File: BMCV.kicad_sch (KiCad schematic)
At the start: 32 parts, among them J13 DebugPins, J14 USB_C_Receptacle_USB2.0_14P, J15 Conn_01x02, SW14 Reset, SW15 Boot, U32 TXS0108EPW, U36 STM32G474CETx, U37 MB85RS64PNF-G-JNERE1, Y1 38.4MHz 10pF

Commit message: update
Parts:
- removed J15: Conn_01x02, TestPoint:TestPoint_2Pads_Pitch2.54mm_Drill0.8mm, symbol PCM_4ms_Connector:Conn_01x02
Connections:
- net PB7 is gone; now on net LEVEL_SHIFTER_EN: U36.44 (PB7)
- net +3.3V: no longer R162.2
- net GND: now also R162.1
- net LEVEL_SHIFTER_EN: now reaches U32.10 (OE)
- net LEVEL_SHIFTER_EN: now also R162.2; no longer R162.1
- net PB6 renamed PWR_ANALOG_EN
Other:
- moved on the sheet: R162

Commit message: first ordered verrsion
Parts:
- added R4: 1k5, Resistor_SMD:R_0603_1608Metric, symbol Device:R_Small
- C1, C2: LCSC Part # C32949 -> C161520
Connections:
- net +3.3VA: now also U36.20 (VREF+)
- net GND: now also VR1.E1 (E_(-))
- net at VR1.B1 (B_(+)): now also R4.2
- net PWR_ANALOG_EN renamed SLIDER_LED
- net SLIDER_LED: now also R4.1
- no-connect marks 6 -> 3
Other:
- note added: "NRST/PG10 has internal pull-up"

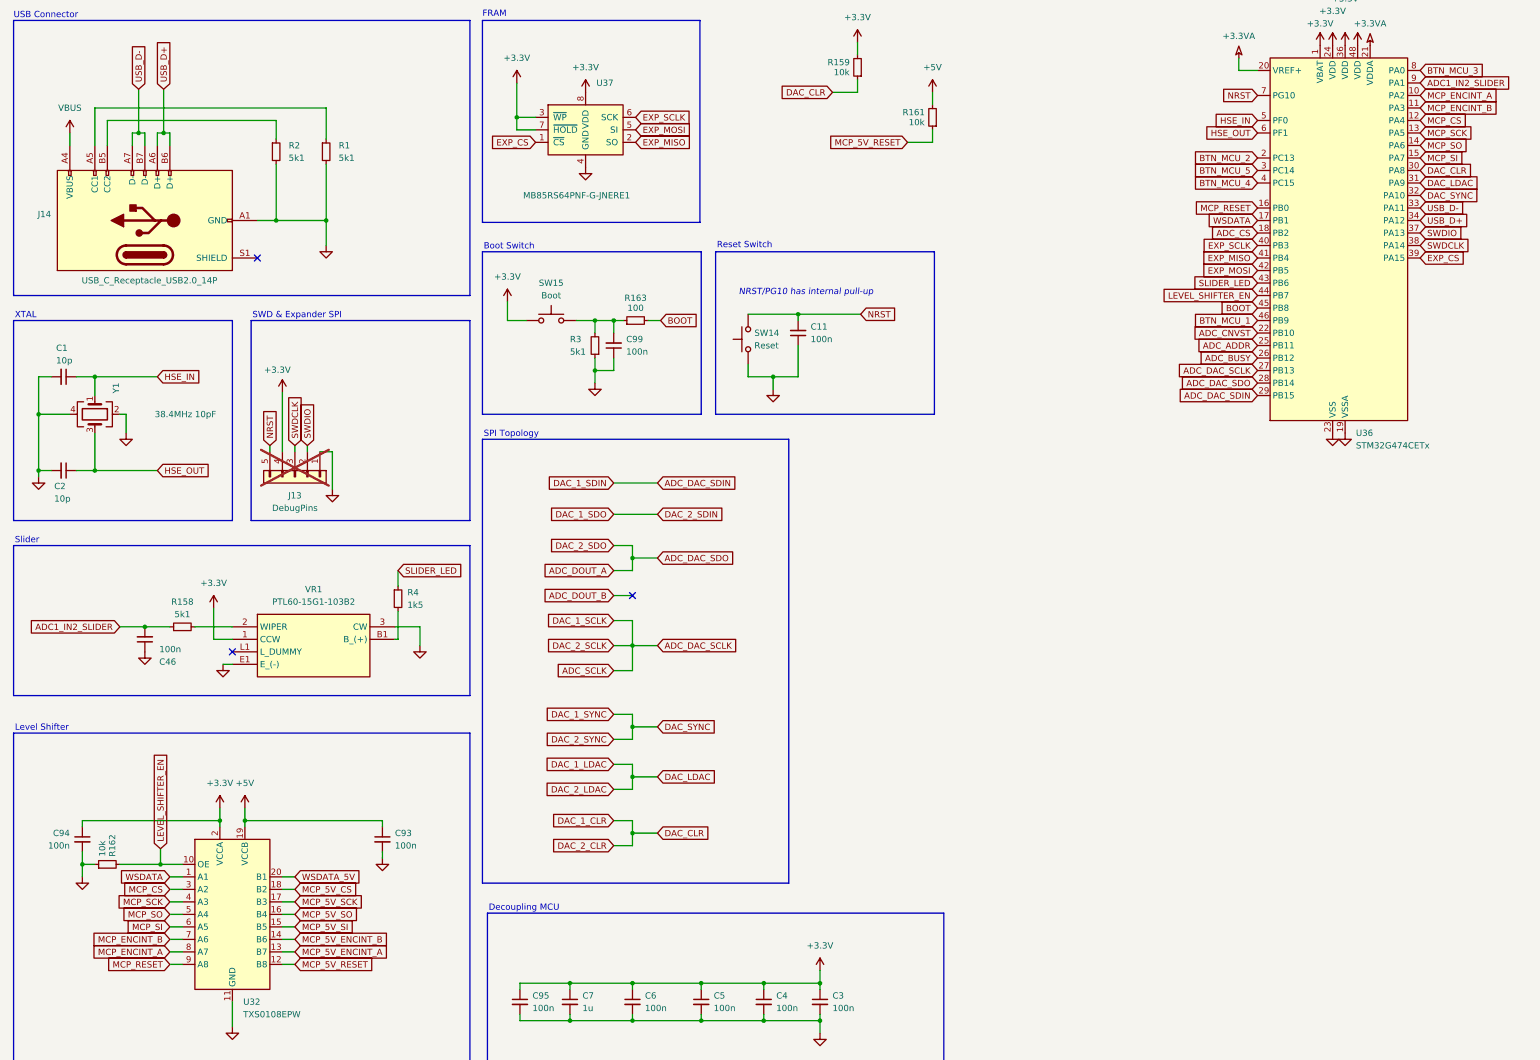
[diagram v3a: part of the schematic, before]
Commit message: add test firwmware
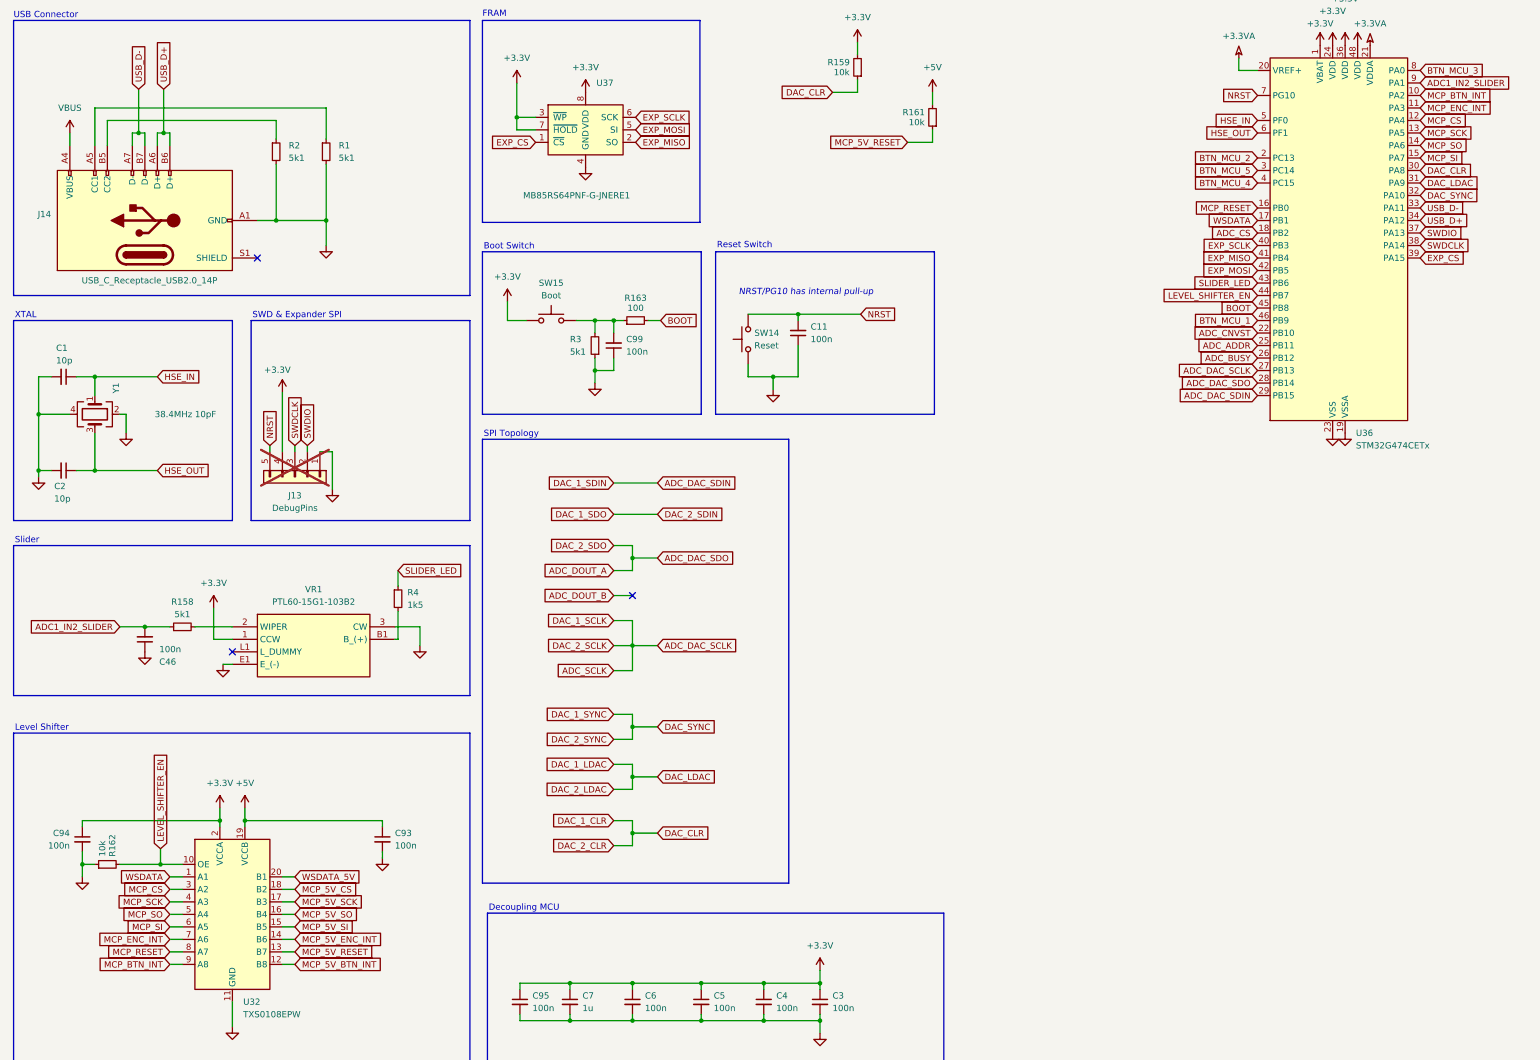
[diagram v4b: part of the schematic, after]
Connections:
- net MCP_5V_ENCINT_A is gone; now on net MCP_5V_RESET: U32.13 (B7)
- net MCP_5V_RESET: no longer U32.12 (B8)
- net MCP_RESET: now also U32.8 (A7); no longer U32.9 (A8)
- net MCP_5V_ENCINT_B renamed MCP_5V_ENC_INT
- net MCP_ENCINT_A renamed MCP_BTN_INT
- net MCP_BTN_INT: now also U32.9 (A8); no longer U32.8 (A7)
- net MCP_ENCINT_B renamed MCP_ENC_INT
- new net MCP_5V_BTN_INT: U32.12 (B8)

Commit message: pcb changes
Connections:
- no-connect marks 3 -> 4
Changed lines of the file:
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@@
 	)
 	(junction
-		(at 140.97 175.26)
-		(diameter 0)
-		(color 0 0 0 0)
-	)
-	(junction
 		(at 29.21 237.49)
 		(diameter 0)
@@
 	)
 	(no_connect
+		(at 140.97 172.72)
+	)
+	(no_connect
 		(at 64.77 114.3)
 	)
@@
 	(wire
 		(pts
-			(xy 140.97 177.8) (xy 137.16 177.8)
+			(xy 137.16 177.8) (xy 146.05 177.8)
 		)
 		(stroke
@@
 	(wire
 		(pts
-			(xy 140.97 172.72) (xy 140.97 175.26)
-		)
-		(stroke
-			(width 0)
-			(type default)
-		)
-	)
-	(wire
-		(pts
 			(xy 118.11 269.24) (xy 128.27 269.24)
 		)
@@
 	(wire
 		(pts
-			(xy 140.97 175.26) (xy 146.05 175.26)
-		)
-		(stroke
-			(width 0)
-			(type default)
-		)
-	)
-	(wire
-		(pts
 			(xy 20.32 157.48) (xy 20.32 146.05)
 		)
@@
 	(wire
 		(pts
-			(xy 140.97 175.26) (xy 140.97 177.8)
-		)
-		(stroke
-			(width 0)
-			(type default)
-		)
-	)
-	(wire
-		(pts
 			(xy 69.85 257.81) (xy 72.39 257.81)
 		)
@@
 	(global_label "ADC_DAC_SDO"
 		(shape input)
-		(at 146.05 175.26 0)
+		(at 146.05 177.8 0)
 		(fields_autoplaced yes)
 		(effects
@@
 		)
 		(property "Intersheetrefs" "${INTERSHEET_REFS}"
-			(at 162.0376 175.26 0)
+			(at 162.0376 177.8 0)
 			(effects
 				(font

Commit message: pcb
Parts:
- added C112: 100n, Capacitor_SMD:C_0402_1005Metric, symbol Device:C_Small
- added U42: 74AHCT1G125, Package_TO_SOT_SMD:SOT-353_SC-70-5, symbol 74xGxx:74AHCT1G125
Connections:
- net +5V: now also C112.1, U42.5 (VCC)
- net GND: now also C112.2, U42.1, U42.3 (GND)
- net WSDATA: now also U42.2; no longer U32.1 (A1)
- net WSDATA_5V: now also U42.4; no longer U32.20 (B1)
- no-connect marks 4 -> 6

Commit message: pcb update
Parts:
- removed R159: 10k, Resistor_SMD:R_0402_1005Metric, symbol Device:R_Small
- added R164: 100, Resistor_SMD:R_0402_1005Metric, symbol Device:R_Small
- added R41: 5k1, Resistor_SMD:R_0402_1005Metric, symbol Device:R_Small
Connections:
- net DAC_1_LDAC is gone; now on net DAC_1_SYNC: U36.31 (PA9)
- net +3.3V: now also SW14.1
- net DAC_1_SYNC: no longer U36.32 (PA10)
- net GND: now also R41.1; no longer SW14.1
- net NRST: no longer C11.2, SW14.2
- net DAC_1_CLR renamed BTN_MENU_2
- net BTN_MENU_2: now also R164.2
- new net: C11.2, R164.1, R41.2, SW14.2
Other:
- moved on the sheet: C11, R163, SW14

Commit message: v1
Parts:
- removed C11, C99: 100n, Capacitor_SMD:C_0402_1005Metric, symbol Device:C_Small
- removed R4: 1k5, Resistor_SMD:R_0603_1608Metric, symbol Device:R_Small
- removed VR1: PTL60-15G1-103B2, BMCV:PTL6015xxxxxxx, symbol BMCV:PTLxx-xxxx-xxxxx
- added J13: EXTRA_PIN_1, TestPoint:TestPoint_Pad_D1.5mm, symbol Connector:Conn_01x01_Pin
- added R159, R160, R165, R166, R167, R169, R170: 10k, Resistor_SMD:R_0402_1005Metric, symbol Device:R_Small
- added R168: 100, Resistor_SMD:R_0402_1005Metric, symbol Device:R_Small
- added RV13: R_Potentiometer_Dual, BMCV:ALPHA_B10KX2, symbol Device:R_Potentiometer_Dual
- added SW16: FN3, BMCV:TS-1095PS-AXXBX-C3DX, symbol Switch:SW_Push
- R158: value 5k1 -> 1k; LCSC Part # C25905 -> C11702
- R3, R41: value 5k1 -> 10k; LCSC Part # C25905 -> C25744
- SW14: value Reset -> FN1
- SW15: value Boot -> FN2/Boot
- renumbered J13 to Jw1
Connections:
- net +3.3V: now also Jw1.2 (Pin_2), R165.1, R166.1, R169.1, R170.1, RV13.1, RV13.4, SW16.1; no longer Jw1.4 (Pin_4), U37.3 (~{WP}), U37.7 (~{HOLD})
- net DAC_1_SYNC: now also U36.32 (PA10); no longer U36.31 (PA9)
- net GND: now also R159.1, R160.1, R167.1, RV13.3, RV13.6
- net SWDCLK: now also Jw1.4 (Pin_4); no longer Jw1.3 (Pin_3)
- net SWDIO: now also Jw1.3 (Pin_3); no longer Jw1.2 (Pin_2)
- net at R158.2: now also RV13.5
- net SLIDER_LED renamed BTN_MENU_3
- net BTN_MENU_3: now also R168.2
- new net: R169.2, U37.7 (~{HOLD})
- new net: R170.2, U37.3 (~{WP})
- new net: R167.2, R168.1, SW16.2
- new net DAC_1_CLR: R165.2
- new net DAC_1_LDAC: R159.2
- new net DAC_2_CLR: R166.2
- new net DAC_2_LDAC: R160.2
- new net EXTRA_PIN_1: J13.1 (Pin_1), U36.31 (PA9)
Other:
- note added: "FN1/Boot Button"
- note added: "FN2 Button"
- note added: "FN3 Button"
- note removed: "Boot Switch"
- note removed: "Reset Switch"
- moved on the sheet: C46, R158, R163, R164, R3, R41, SW14, SW15
